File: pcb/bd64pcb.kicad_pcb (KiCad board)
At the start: 2 copper layers, 266.7 x 95.2 mm, 225 parts, among them J1 USB_C_Receptacle_USB2.0, SW1 SW_Push, U1 ATmega32U4-MU, U3 IS31FL3733-QF, Y1 16MHz

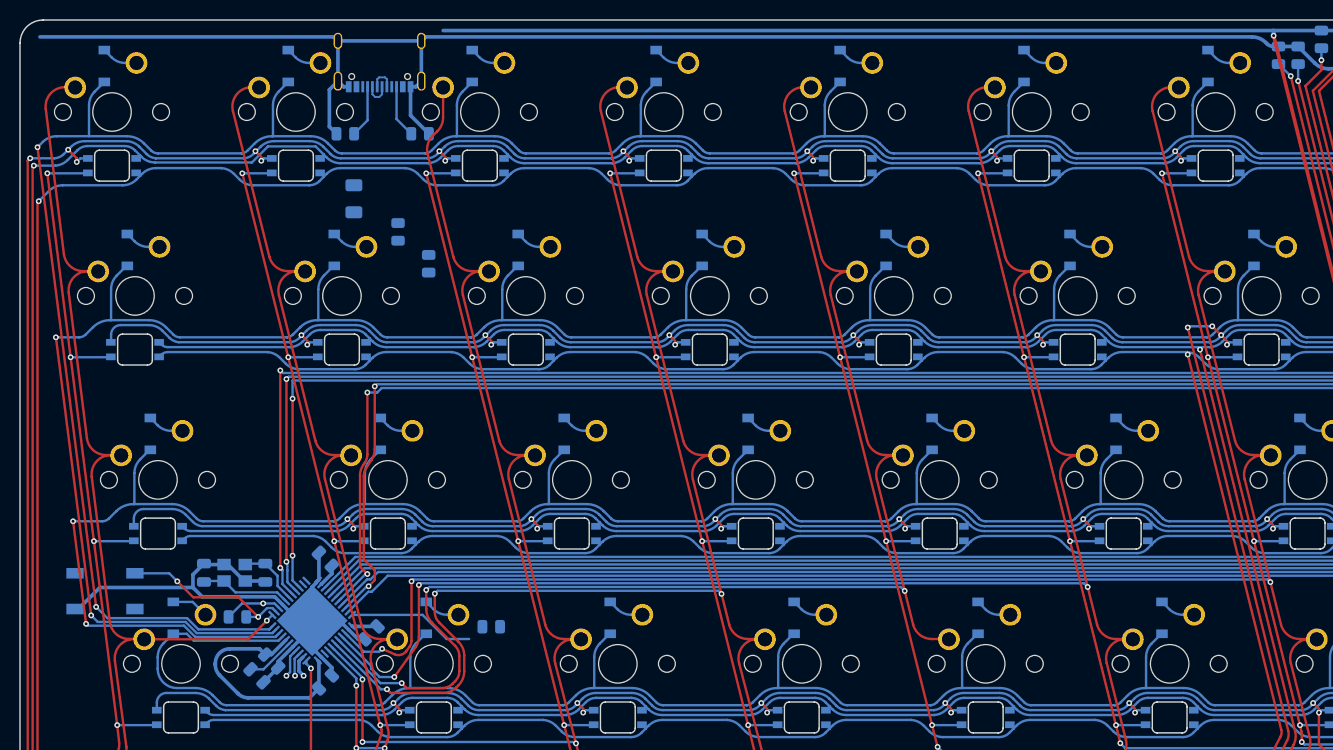
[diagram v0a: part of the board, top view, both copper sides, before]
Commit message: change and relocate usbc footprint
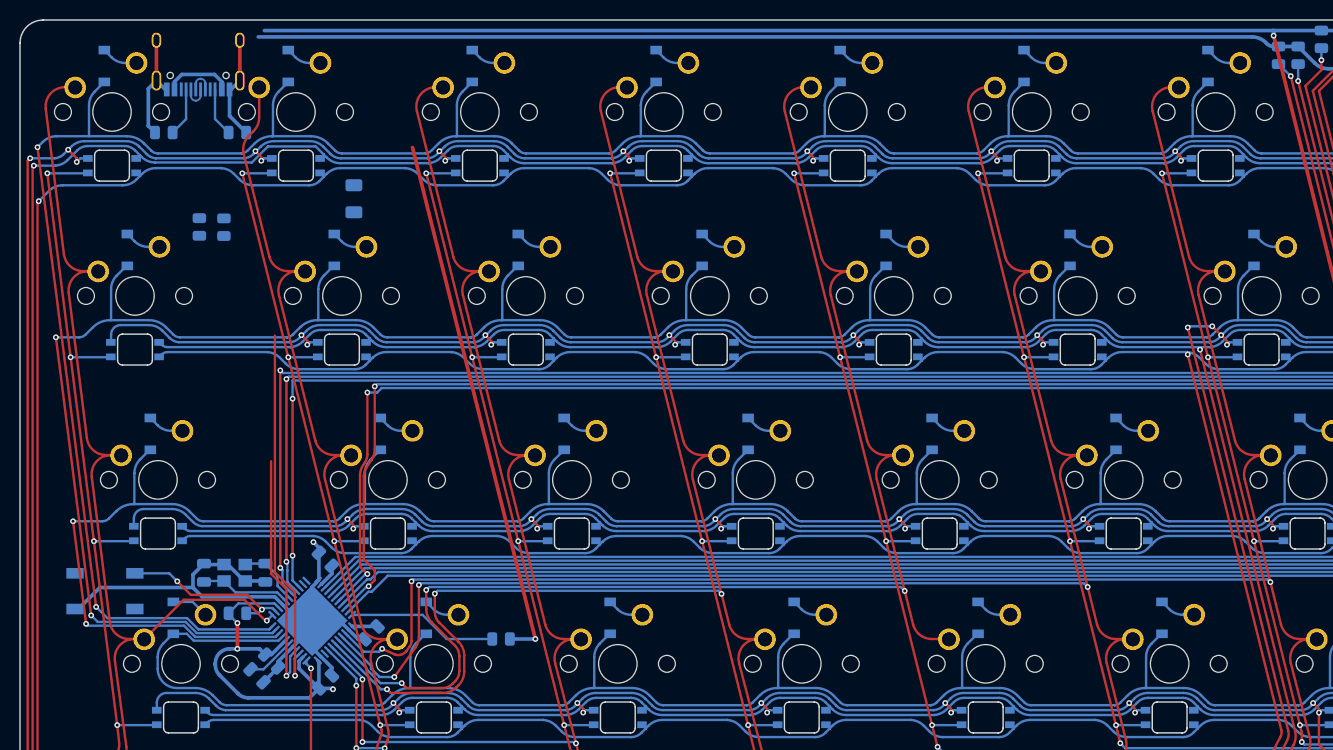
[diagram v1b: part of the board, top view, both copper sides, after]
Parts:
- J1: footprint Connector_USB:USB_C_Receptacle_Palconn_UTC16-G -> Connector_USB:USB_C_Receptacle_HRO_TYPE-C-31-M-12
- moved R4 21.5 mm to (36.2, 63.5)
- moved R8 20.6 mm to (33.7, 63.5)
- moved R2 18.9 mm to (37.6, 53.7)
- moved J1 18.8 mm to (33.5, 45.2)
- moved R1 18.8 mm to (30.0, 53.7)
- moved R9 1.63 mm to (64.9, 106.2)
- moved R3 0.38 mm to (37.6, 103.5)
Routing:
- net Net-(R8-Pad1): track 2.53 -> 38.6 mm
- net GND: track 377.4 -> 410.5 mm, vias 4 -> 6
- net +5V: track 404.4 -> 430.2 mm, vias 15 -> 16
- net Net-(R4-Pad1): track 3.07 -> 26.0 mm
- net VCC: track 0.00 -> 7.12 mm
- net Net-(R9-Pad2): track 13.2 -> 15.6 mm
- net col0: track 107.9 -> 109.7 mm
- net col2: track 125.5 -> 127.0 mm
- net col1: track 111.1 -> 109.6 mm

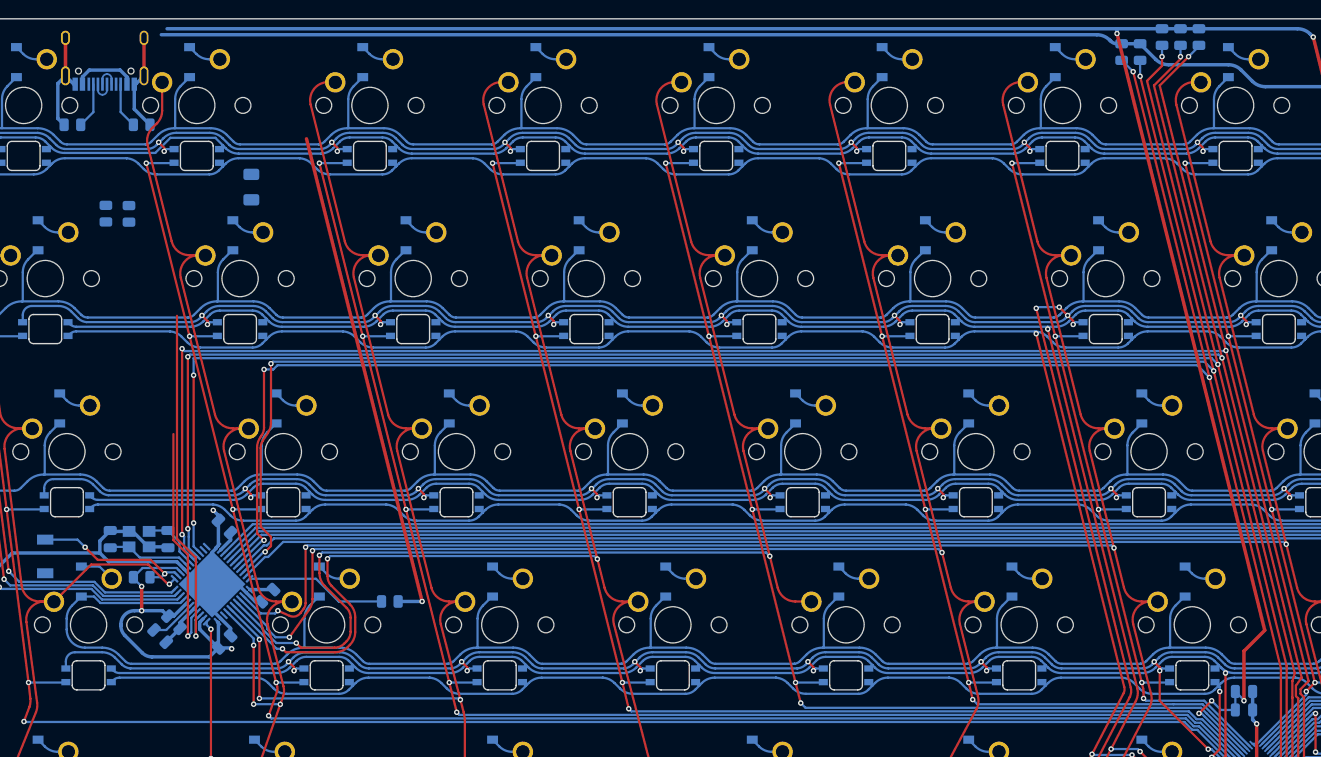
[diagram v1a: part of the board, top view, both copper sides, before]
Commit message: clean usbc footprint and some fillets
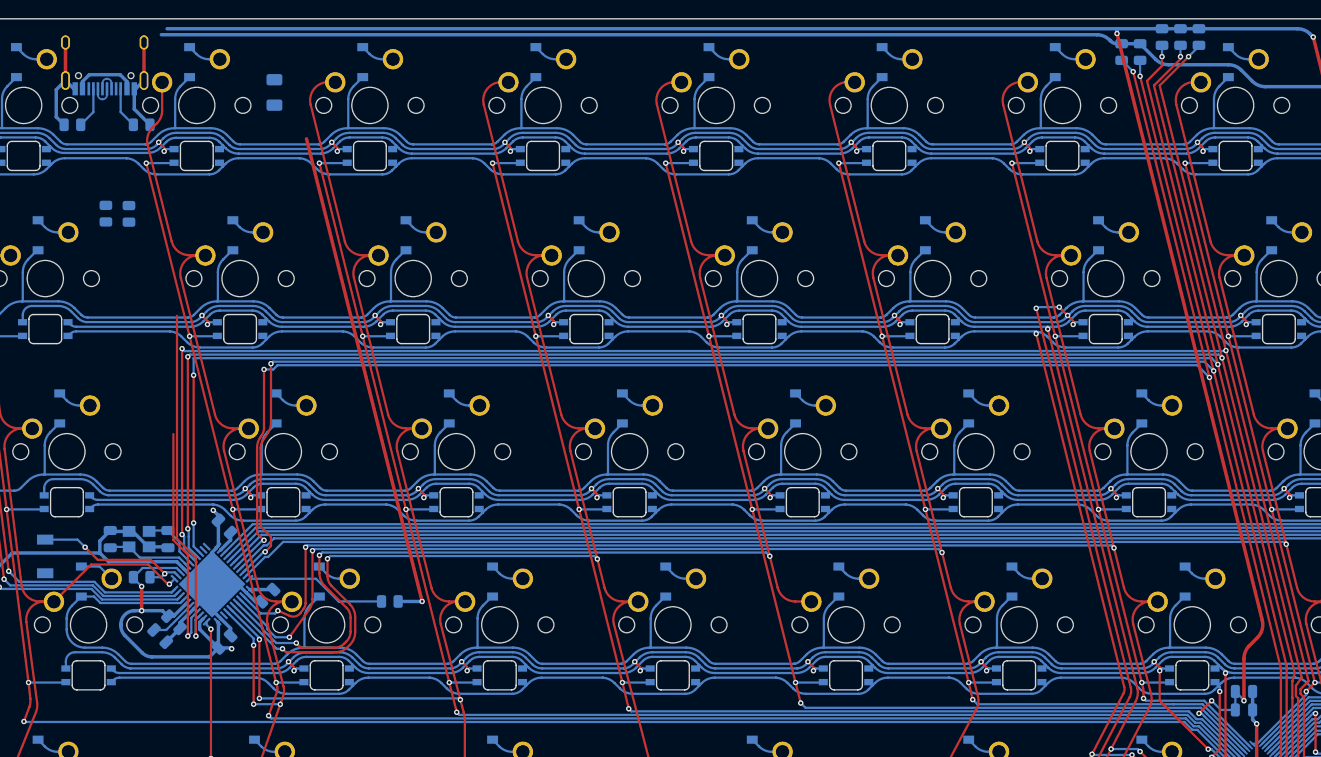
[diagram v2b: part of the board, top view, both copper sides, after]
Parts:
- moved F1 10.7 mm to (52.2, 50.2)
- moved J1 0.51 mm to (33.5, 45.7)
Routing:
- net GND: track 410.5 -> 409.6 mm
- net Net-(J1-PadB5): track 5.04 -> 4.54 mm
- net Net-(J1-PadA5): track 5.04 -> 4.53 mm

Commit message: bd logo on pcb
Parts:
- added G***: LOGO, BD:BD_logo, F.Cu at (148.4, 89.7)

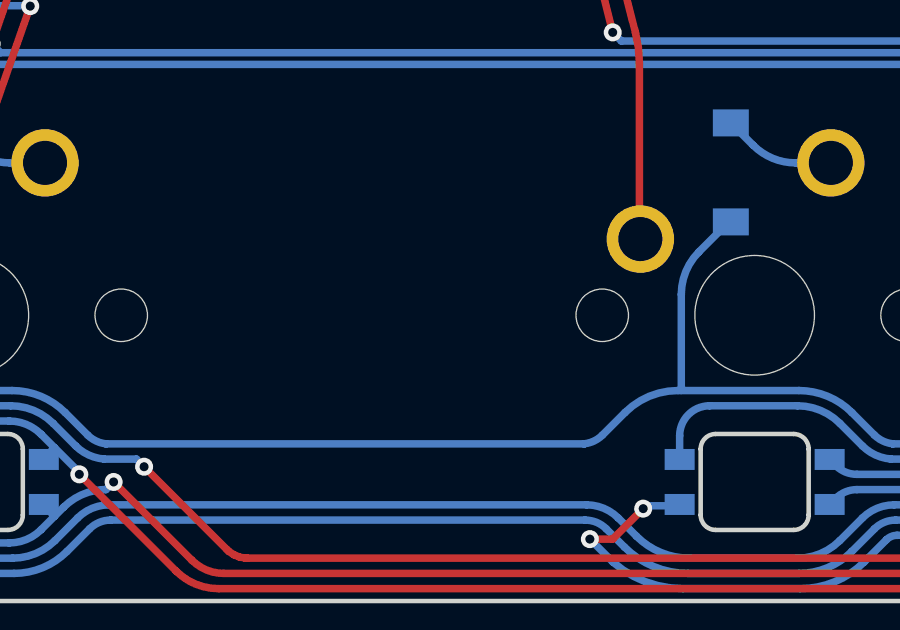
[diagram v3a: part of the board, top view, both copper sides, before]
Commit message: silk text to jlc spec
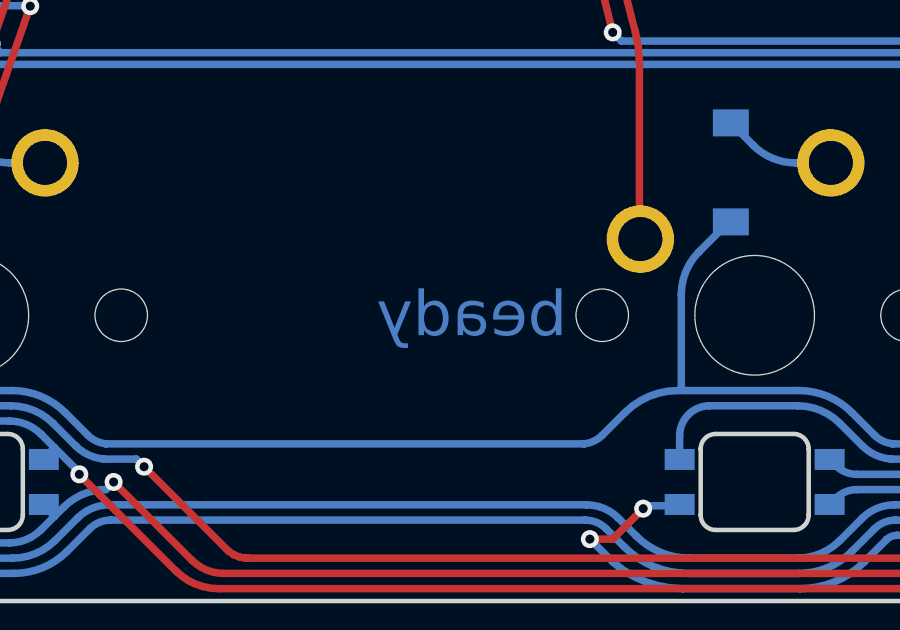
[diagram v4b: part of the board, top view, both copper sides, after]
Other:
- board text added: "ATMEGA32U4"
- board text added: "IS31FL3733B"
- board text added: "beady"
- board text added: "biddle"
- board text added: "cols highway"
- board text added: "i2c highway"
- board text added: "tantalum"

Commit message: vanity silk
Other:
- board text added: "64"
- board text added: "QBLP677R-RGB"
- board text added: "bd"
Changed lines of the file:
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@@
     (effects (font (size 1.5 1.5) (thickness 0.3)) (justify left mirror))
   )
-  (gr_text "cols highway" (at 117.602 99.06) (layer "B.SilkS")
+  (gr_text "bd" (at 42.672 127.635) (layer "B.Cu")
+    (effects (font (size 2 2) (thickness 0.4)) (justify left mirror))
+  )
+  (gr_text "cols highway" (at 150.749 98.552) (layer "B.SilkS")
     (effects (font (size 1 1) (thickness 0.2)) (justify mirror))
   )
@@
     (effects (font (size 1 1) (thickness 0.2)) (justify mirror))
   )
+  (gr_text "QBLP677R-RGB" (at 272.161 59.69) (layer "B.SilkS")
+    (effects (font (size 1 1) (thickness 0.2)) (justify mirror))
+  )
+  (gr_text "64" (at 39.116 127.635) (layer "B.SilkS")
+    (effects (font (size 2 2) (thickness 0.4)) (justify left mirror))
+  )
   (gr_text "ATMEGA32U4" (at 43.434 113.919) (layer "B.SilkS")
     (effects (font (size 1 1) (thickness 0.2)) (justify mirror))
   )
+  (gr_text "bd" (at 42.672 127.635) (layer "B.Mask")
+    (effects (font (size 2 2) (thickness 0.4)) (justify left mirror))
+  )
   (gr_text "beady" (at 70.739 127.762) (layer "B.Mask")

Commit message: more informative silk
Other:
- board text added: "SW1/2/3, CS16/15"
- board text added: "SW10/11/12, CS16/15/14"
- board text added: "SW4/5/6, CS16/15/14"
- board text added: "SW7/8/9, CS16/15/14"
- board text removed: "cols highway"
- board text removed: "i2c highway"
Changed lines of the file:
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@@
     (effects (font (size 2 2) (thickness 0.4)) (justify left mirror))
   )
-  (gr_text "cols highway" (at 150.749 98.552) (layer "B.SilkS")
+  (gr_text "SW7/8/9, CS16/15/14" (at 172.212 135.89) (layer "B.SilkS")
     (effects (font (size 1 1) (thickness 0.2)) (justify mirror))
   )
@@
     (effects (font (size 1 1) (thickness 0.2)) (justify mirror))
   )
-  (gr_text "i2c highway" (at 150.368 79.375) (layer "B.SilkS")
-    (effects (font (size 1 1) (thickness 0.2)) (justify mirror))
-  )
   (gr_text "QBLP677R-RGB" (at 272.161 59.69) (layer "B.SilkS")
     (effects (font (size 1 1) (thickness 0.2)) (justify mirror))
@@
     (effects (font (size 2 2) (thickness 0.4)) (justify left mirror))
   )
+  (gr_text "SW10/11/12, CS16/15/14" (at 245.999 135.89) (layer "B.SilkS")
+    (effects (font (size 1 1) (thickness 0.2)) (justify mirror))
+  )
+  (gr_text "SW1/2/3, CS16/15" (at 38.227 135.89) (layer "B.SilkS")
+    (effects (font (size 1 1) (thickness 0.2)) (justify mirror))
+  )
   (gr_text "ATMEGA32U4" (at 43.434 113.919) (layer "B.SilkS")
     (effects (font (size 1 1) (thickness 0.2)) (justify mirror))
   )
+  (gr_text "SW4/5/6, CS16/15/14" (at 105.537 135.89) (layer "B.SilkS")
+    (effects (font (size 1 1) (thickness 0.2)) (justify mirror))
+  )

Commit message: everything connected and all errors/warnings resolved
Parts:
- moved F1 35.9 mm to (40.0, 83.9)
- moved R4 10.7 mm to (34.8, 53.0)
- moved R8 10.6 mm to (32.8, 53.0)
- moved C4 1.08 mm to (47.8, 110.9)
- moved C1 0.27 mm to (46.6, 98.2)
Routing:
- net +5V: track 429.9 -> 521.4 mm, vias 16 -> 21
- net GND: track 409.6 -> 499.0 mm, vias 6 -> 8
- net Net-(R4-Pad1): track 26.0 -> 65.0 mm, vias 1 -> 2
- net VCC: track 7.12 -> 42.8 mm, vias 0 -> 2
- net Net-(R8-Pad1): track 38.6 -> 63.0 mm, vias 1 -> 2
- net D+: track 2.75 -> 5.21 mm
- net CS2: track 183.2 -> 185.4 mm
- net D-: track 2.85 -> 4.99 mm
- net Net-(R9-Pad2): track 15.6 -> 17.2 mm
- net col1: track 109.6 -> 110.1 mm

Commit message: fillet touchups
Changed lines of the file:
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@@
   (segment (start 40.288292 102.967708) (end 41.211281 102.967708) (width 0.25) (layer "B.Cu") (net 121))
   (segment (start 30.535 99.369) (end 26.976 99.369) (width 0.25) (layer "B.Cu") (net 121))
-  (segment (start 34.798 55.245) (end 34.798 58.123136) (width 0.25) (layer "F.Cu") (net 122))
-  (segment (start 36.323927 90.742534) (end 36.358112 91.002216) (width 0.25) (layer "F.Cu") (net 122))
-  (segment (start 44.15085 99.861232) (end 44.193581 100.185833) (width 0.25) (layer "F.Cu") (net 122))
-  (segment (start 36.907787 92.025787) (end 43.463767 98.581767) (width 0.25) (layer "F.Cu") (net 122))
-  (segment (start 36.52613 91.497201) (end 36.657089 91.724033) (width 0.25) (layer "F.Cu") (net 122))
-  (segment (start 44.196 100.349534) (end 44.196 110.617) (width 0.25) (layer "F.Cu") (net 122))
-  (segment (start 43.463767 98.581767) (end 43.577824 98.699217) (width 0.25) (layer "F.Cu") (net 122))
-  (segment (start 34.798 58.123136) (end 36.322 59.647136) (width 0.25) (layer "F.Cu") (net 122))
   (segment (start 36.358112 91.002216) (end 36.425899 91.255215) (width 0.25) (layer "F.Cu") (net 122))
   (segment (start 36.816535 91.931832) (end 36.907787 92.025787) (width 0.25) (layer "F.Cu") (net 122))
+  (segment (start 44.066117 99.544985) (end 44.15085 99.861232) (width 0.25) (layer "F.Cu") (net 122))
+  (segment (start 36.52613 91.497201) (end 36.657089 91.724033) (width 0.25) (layer "F.Cu") (net 122))
+  (segment (start 36.907787 92.025787) (end 43.463767 98.581767) (width 0.25) (layer "F.Cu") (net 122))
+  (segment (start 36.322 60.518427) (end 36.322 90.611573) (width 0.25) (layer "F.Cu") (net 122))
+  (segment (start 44.193581 100.185833) (end 44.196 100.349534) (width 0.25) (layer "F.Cu") (net 122))
+  (segment (start 43.577824 98.699217) (end 43.777131 98.958965) (width 0.25) (layer "F.Cu") (net 122))
+  (segment (start 34.798 55.245) (end 34.798 57.337573) (width 0.25) (layer "F.Cu") (net 122))
+  (segment (start 43.463767 98.581767) (end 43.577824 98.699217) (width 0.25) (layer "F.Cu") (net 122))
+  (segment (start 44.15085 99.861232) (end 44.193581 100.185833) (width 0.25) (layer "F.Cu") (net 122))
+  (segment (start 43.940829 99.242504) (end 44.066117 99.544985) (width 0.25) (layer "F.Cu") (net 122))
   (segment (start 36.425899 91.255215) (end 36.52613 91.497201) (width 0.25) (layer "F.Cu") (net 122))
-  (segment (start 43.577824 98.699217) (end 43.777131 98.958965) (width 0.25) (layer "F.Cu") (net 122))
-  (segment (start 36.322 59.647136) (end 36.322 90.611573) (width 0.25) (layer "F.Cu") (net 122))
-  (segment (start 44.066117 99.544985) (end 44.15085 99.861232) (width 0.25) (layer "F.Cu") (net 122))
+  (segment (start 44.196 100.349534) (end 44.196 110.617) (width 0.25) (layer "F.Cu") (net 122))
+  (segment (start 35.383787 58.751787) (end 35.736214 59.104214) (width 0.25) (layer "F.Cu") (net 122))
+  (segment (start 36.322 90.611573) (end 36.323927 90.742534) (width 0.25) (layer "F.Cu") (net 122))
   (segment (start 36.657089 91.724033) (end 36.816535 91.931832) (width 0.25) (layer "F.Cu") (net 122))
-  (segment (start 36.322 90.611573) (end 36.323927 90.742534) (width 0.25) (layer "F.Cu") (net 122))
-  (segment (start 44.193581 100.185833) (end 44.196 100.349534) (width 0.25) (layer "F.Cu") (net 122))
-  (segment (start 43.940829 99.242504) (end 44.066117 99.544985) (width 0.25) (layer "F.Cu") (net 122))
   (segment (start 43.777131 98.958965) (end 43.940829 99.242504) (width 0.25) (layer "F.Cu") (net 122))
+  (segment (start 36.323927 90.742534) (end 36.358112 91.002216) (width 0.25) (layer "F.Cu") (net 122))
   (via (at 44.196 110.617) (size 0.6) (drill 0.3) (layers "F.Cu" "B.Cu") (net 122))
   (via (at 34.798 55.245) (size 0.6) (drill 0.3) (layers "F.Cu" "B.Cu") (net 122))
+  (arc (start 34.798 57.337573) (mid 34.950241 58.10294) (end 35.383787 58.751787) (width 0.25) (layer "F.Cu") (net 122))
+  (arc (start 36.322 60.518427) (mid 36.169759 59.75306) (end 35.736214 59.104214) (width 0.25) (layer "F.Cu") (net 122))
   (segment (start 42.996489 108.023725) (end 43.686138 107.334076) (width 0.25) (layer "B.Cu") (net 122))
   (segment (start 42.996489 110.117) (end 42.996489 108.023725) (width 0.25) (layer "B.Cu") (net 122))
@@
   (segment (start 42.29952 78.62152) (end 156.83648 78.62152) (width 0.25) (layer "B.Cu") (net 125))
   (segment (start 153.924 45.085) (end 152.781 46.228) (width 0.25) (layer "B.Cu") (net 125))
-  (segment (start 32.766 55.245) (end 32.766 56.642) (width 0.25) (layer "F.Cu") (net 126))
-  (segment (start 43.688 109.855) (end 43.561 109.982) (width 0.25) (layer "F.Cu") (net 126))
-  (segment (start 32.766 56.642) (end 35.814 59.69) (width 0.25) (layer "F.Cu") (net 126))
-  (segment (start 35.814 59.69) (end 35.814 90.616398) (width 0.25) (layer "F.Cu") (net 126))
+  (segment (start 33.351787 57.481787) (end 35.37466 59.50466) (width 0.25) (layer "F.Cu") (net 126))
   (segment (start 36.546233 92.384165) (end 43.102214 98.940146) (width 0.25) (layer "F.Cu") (net 126))
   (segment (start 43.688 100.354359) (end 43.688 109.855) (width 0.25) (layer "F.Cu") (net 126))
+  (segment (start 35.814 60.56532) (end 35.814 90.616398) (width 0.25) (layer "F.Cu") (net 126))
+  (segment (start 43.688 109.855) (end 43.561 109.982) (width 0.25) (layer "F.Cu") (net 126))
+  (segment (start 32.766 55.245) (end 32.766 56.067573) (width 0.25) (layer "F.Cu") (net 126))
   (via (at 32.766 55.245) (size 0.6) (drill 0.3) (layers "F.Cu" "B.Cu") (net 126))
   (via (at 43.561 109.982) (size 0.6) (drill 0.3) (layers "F.Cu" "B.Cu") (net 126))
+  (arc (start 32.766 56.067573) (mid 32.918241 56.83294) (end 33.351787 57.481787) (width 0.25) (layer "F.Cu") (net 126))
+  (arc (start 35.814 90.616398) (mid 36.004301 91.573107) (end 36.546233 92.384165) (width 0.25) (layer "F.Cu") (net 126))
   (arc (start 43.102214 98.940146) (mid 43.535759 99.588992) (end 43.688 100.354359) (width 0.25) (layer "F.Cu") (net 126))
-  (arc (start 35.814 90.616398) (mid 36.004301 91.573107) (end 36.546233 92.384165) (width 0.25) (layer "F.Cu") (net 126))
+  (arc (start 35.37466 59.50466) (mid 35.699819 59.991295) (end 35.814 60.56532) (width 0.25) (layer "F.Cu") (net 126))
   (segment (start 32.766 55.245) (end 32.766 53.8715) (width 0.25) (layer "B.Cu") (net 126))
   (segment (start 44.039691 107.687629) (end 43.519188 108.208132) (width 0.25) (layer "B.Cu") (net 126))
